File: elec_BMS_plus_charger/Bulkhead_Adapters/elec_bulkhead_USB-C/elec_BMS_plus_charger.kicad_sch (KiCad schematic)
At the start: 15 parts, among them J1 JST EH 2, J2 USB-C Rec. Vert.

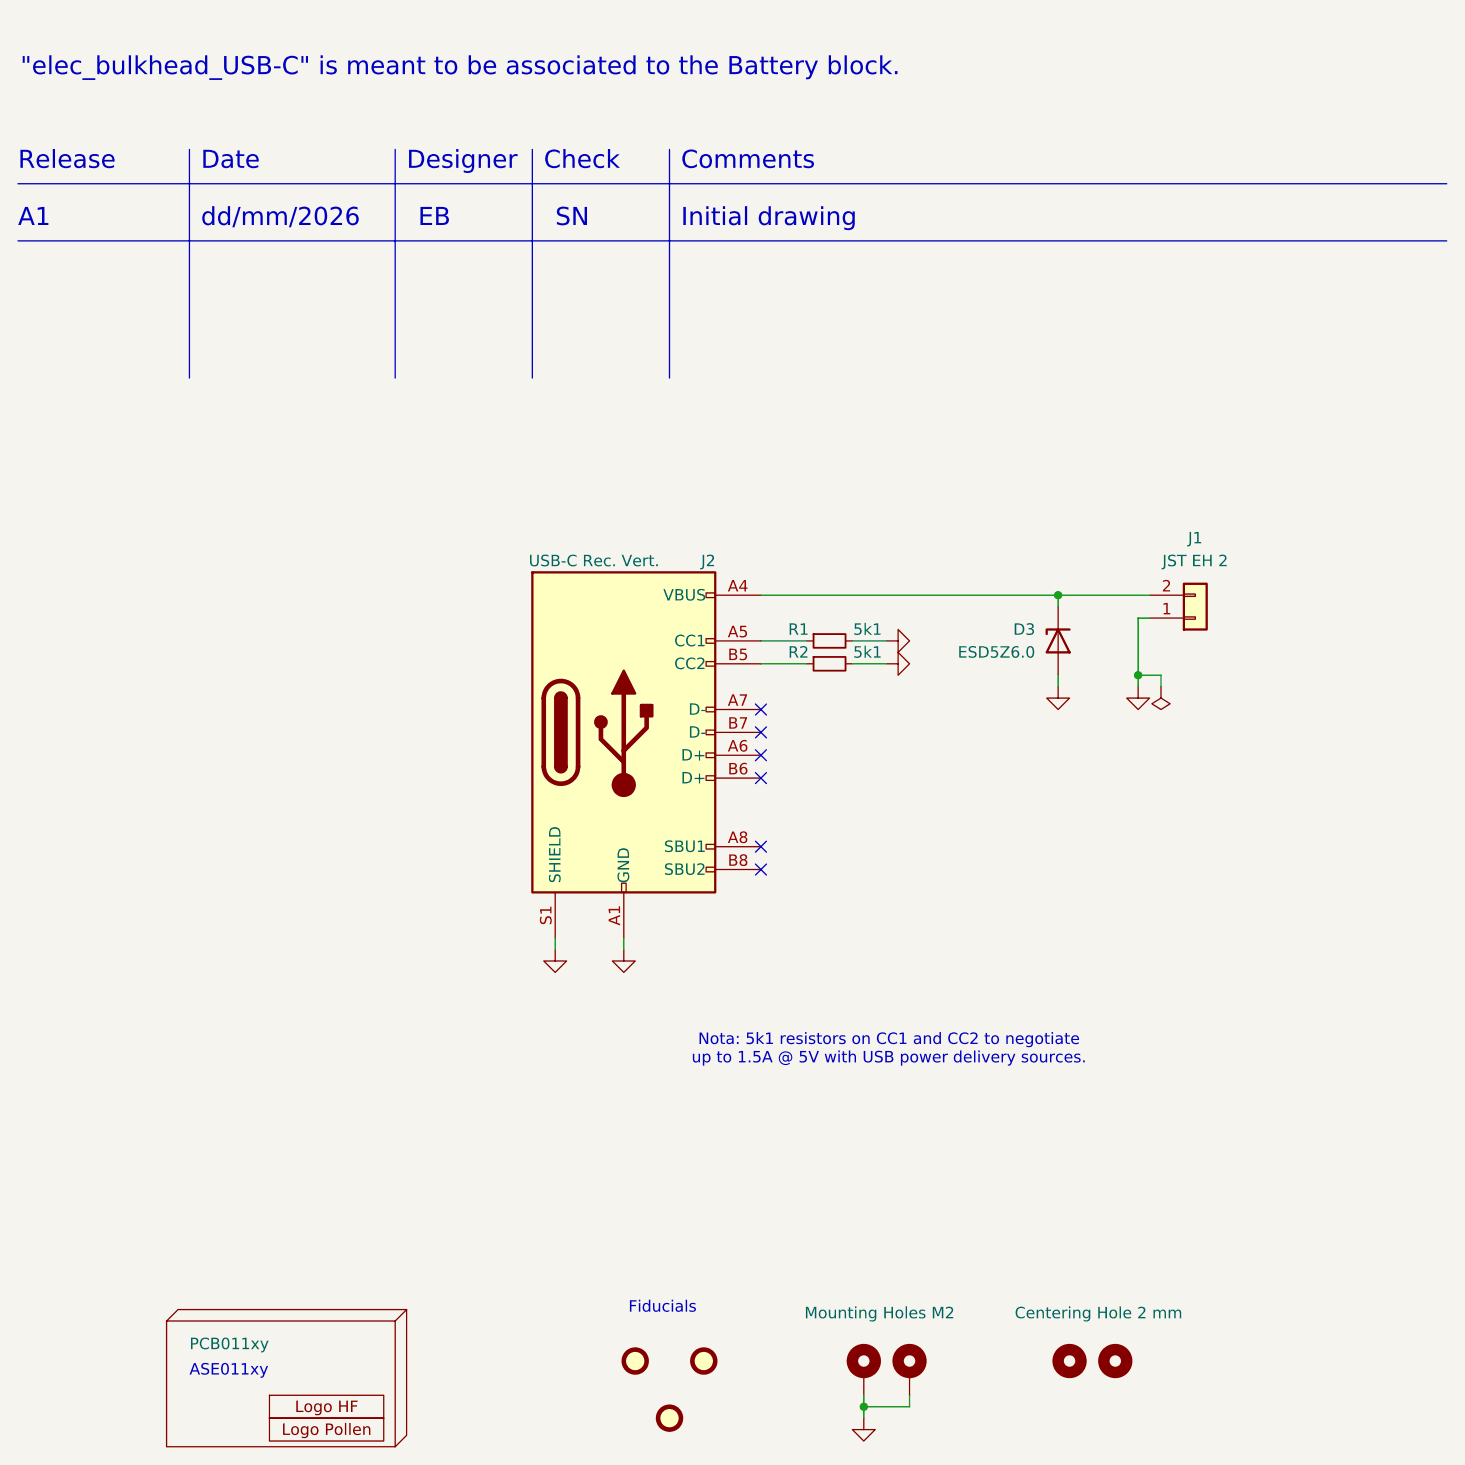
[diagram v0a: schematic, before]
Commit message: [added] XT60-USB-C Bulkhead for Gripette, JLC ready.
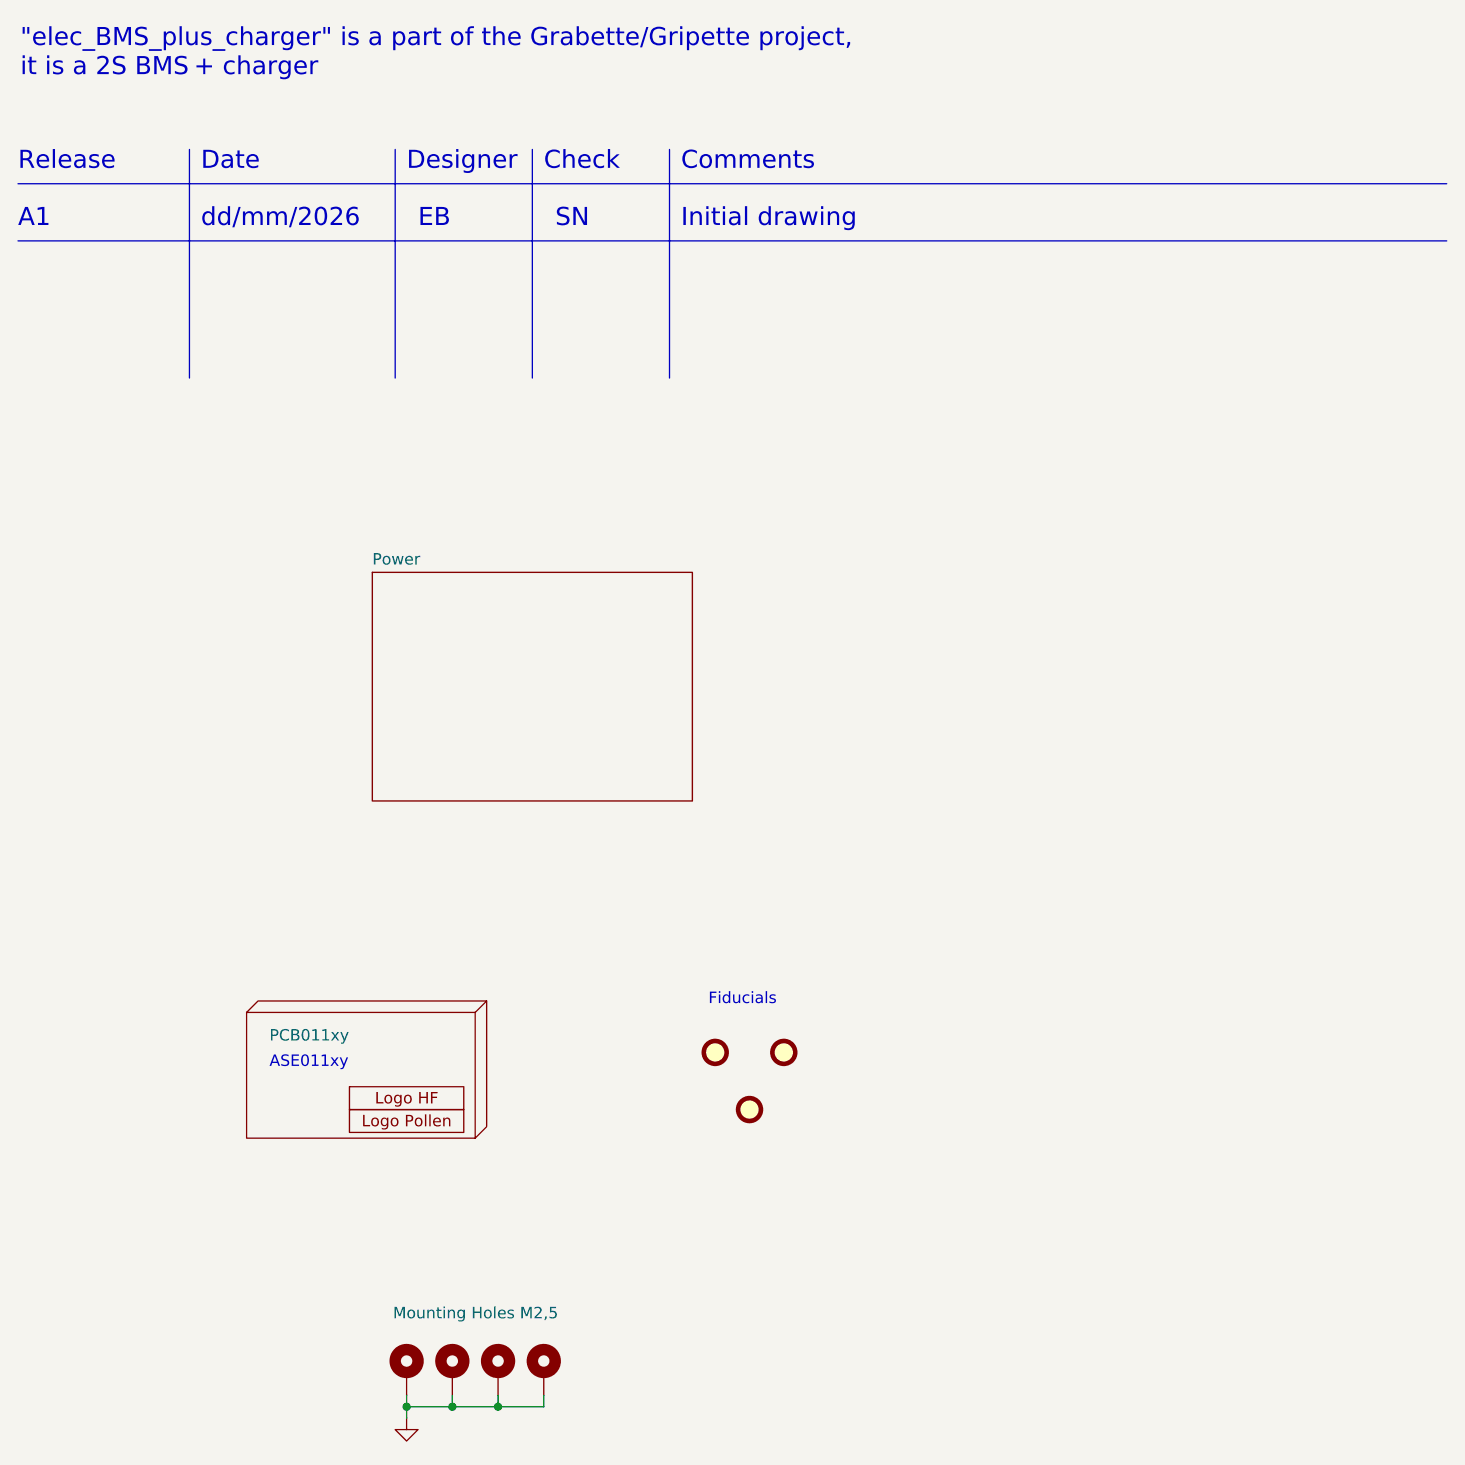
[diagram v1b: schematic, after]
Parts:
- removed D3: ESD5Z6.0, Diode_SMD:D_SOD-523, symbol Diode:ESD5Zxx
- removed H6, H7: Centering Hole 2 mm, Library_Pollen:MountingHole_2.0mm, symbol Mechanical:MountingHole
- removed J1: JST EH 2, Connector_JST:JST_EH_B2B-EH-A_1x02_P2.50mm_Vertical, symbol Connector_Generic:Conn_01x02
- removed J2: USB-C Rec. Vert., Library_Pollen:USB-C_16p_vert_Shou-Han_TYPE-C 16P LTH6.8 - C5187468, symbol Connector:USB_C_Receptacle_USB2.0_16P
- removed R1, R2: 5k1, Resistor_SMD:R_0402_1005Metric, symbol Device:R_Small
- added H6, H7: Mounting Holes M2,5, MountingHole:MountingHole_2.7mm_M2.5_ISO7380_Pad_TopBottom, symbol Mechanical:MountingHole_Pad
- H4, H5: value Mounting Holes M2 -> Mounting Holes M2,5; footprint MountingHole:MountingHole_2.2mm_M2_ISO7380_Pad_TopBottom -> MountingHole:MountingHole_2.7mm_M2.5_ISO7380_Pad_TopBottom
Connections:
- net GND: now also H6.1, H7.1
- no-connect marks 6 -> 0
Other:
- added sheet Power (power.kicad_sch)
- note added: ""elec_BMS_plus_charger" is a part of the Grabette/Gripette project, it is a 2S BMS + charger"
- note removed: ""elec_bulkhead_USB-C" is meant to be associated to the Battery block."
- note removed: "Nota: 5k1 resistors on CC1 and CC2 to negotiate up to 1.5A @ 5V with USB power delivery sources."
- title: Grabette - USB-C Bulkhead for Battery Bloc -> Grabette - BMS + charger
